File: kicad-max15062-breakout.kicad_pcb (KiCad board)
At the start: 2 copper layers, 35 x 25 mm, 10 parts, among them J1 Input, J2 Output, J3 Mode, U1 MAX15062A

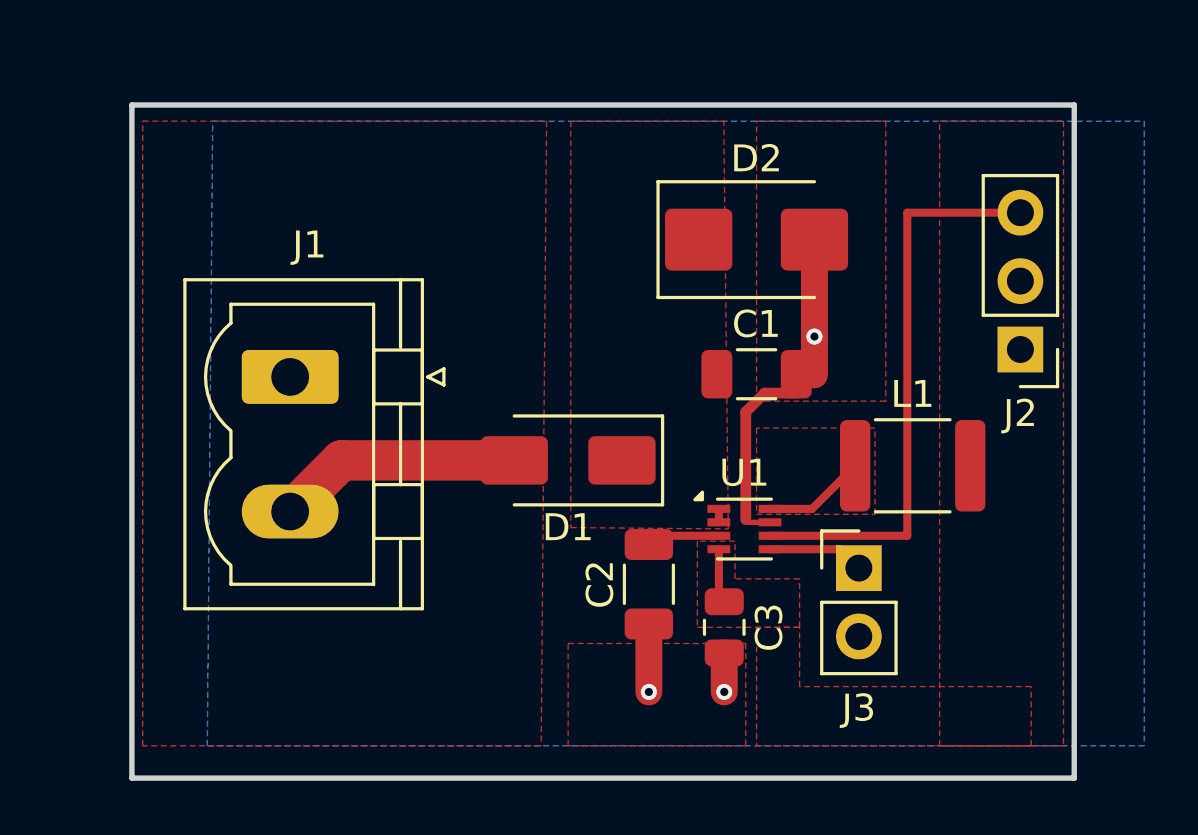
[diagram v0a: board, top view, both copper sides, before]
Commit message: Improved PCB layout and added text to silkscreen
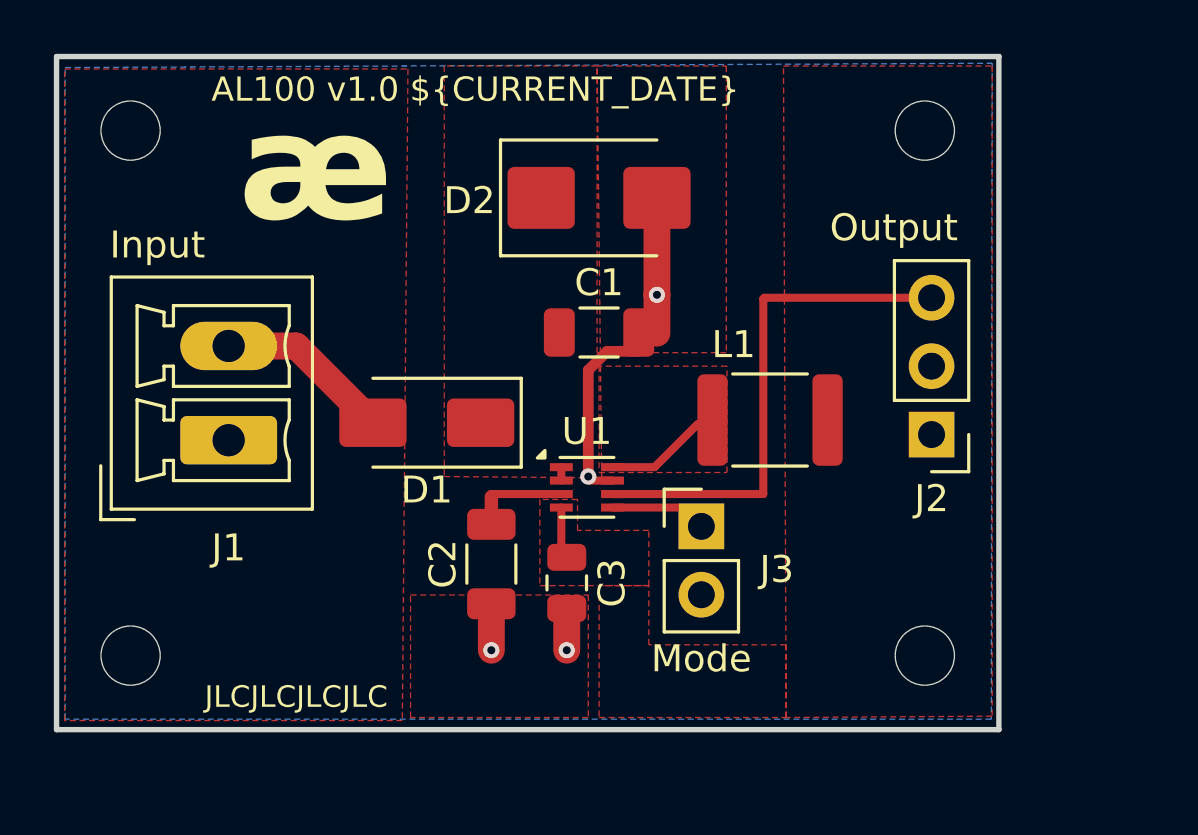
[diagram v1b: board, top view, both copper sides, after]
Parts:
- added H1: MountingHole, MountingHole:MountingHole_2.2mm_M2, F.Cu at (47.8, 57.8)
- added H2: MountingHole, MountingHole:MountingHole_2.2mm_M2, F.Cu at (77.2, 57.8)
- added H3: MountingHole, MountingHole:MountingHole_2.2mm_M2, F.Cu at (47.8, 77.2)
- added H4: MountingHole, MountingHole:MountingHole_2.2mm_M2, F.Cu at (77.2, 77.2)
- J1: footprint Connector_Phoenix_MSTB:PhoenixContact_MSTBVA_2,5_2-G_1x02_P5.00mm_Vertical -> Connector_Phoenix_MC:PhoenixContact_MCV_1,5_2-G-3.5_1x02_P3.50mm_Vertical
- moved C3 6.08 mm to (64.0, 74.5)
- moved C1 6.05 mm to (65.2, 65.2)
- moved D2 6.05 mm to (65.2, 60.2)
- moved J3 6.05 mm to (69.0, 72.5)
- moved U1 6.05 mm to (64.7, 71.0)
- moved C2 5.90 mm to (61.1, 73.8)
- moved L1 5.57 mm to (71.5, 68.5)
- moved D1 5.43 mm to (58.8, 68.6)
- moved J2 4.57 mm to (77.5, 69.0)
- moved J1 3.28 mm to (51.4, 69.2), turned to 90 degrees
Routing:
- net Net-(J2-Pin_3): track 21.3 -> 19.1 mm
- net GND: track 16.9 -> 16.1 mm, vias 3 -> 4
- net Net-(D1-A): track 9.11 -> 8.44 mm
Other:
- board text added: "AL100 v1.0 ${CURRENT_DATE}"
- board text added: "JLCJLCJLCJLC"
- board text added: "æ"
